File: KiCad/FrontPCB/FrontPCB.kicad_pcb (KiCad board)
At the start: 2 copper layers, 38.1 x 38.1 mm, 18 parts, among them U1 ESP32-S3-WROOM-1

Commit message: CHG: changed wiring of front PCB
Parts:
- removed C1, C3, C5, C7: 0.1µF, Capacitor_SMD:C_0805_2012Metric
- moved R1 41.2 mm to (121.9, 54.6), turned to 90 degrees
- moved C8 27.4 mm to (108.0, 58.4), turned to 180 degrees
- moved C2 18.9 mm to (134.6, 55.9), turned to 0 degrees
- moved C6 18.2 mm to (106.7, 83.8), turned to 180 degrees
- moved C4 14.2 mm to (133.3, 81.3), turned to 0 degrees
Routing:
- net +3.3V: track 64.9 -> 109.2 mm
- net GND: track 98.8 -> 125.9 mm
- net unconnected-(R1-Pad1): track 0.00 -> 5.44 mm
- net Net-(D1-DIN): track 0.00 -> 4.10 mm

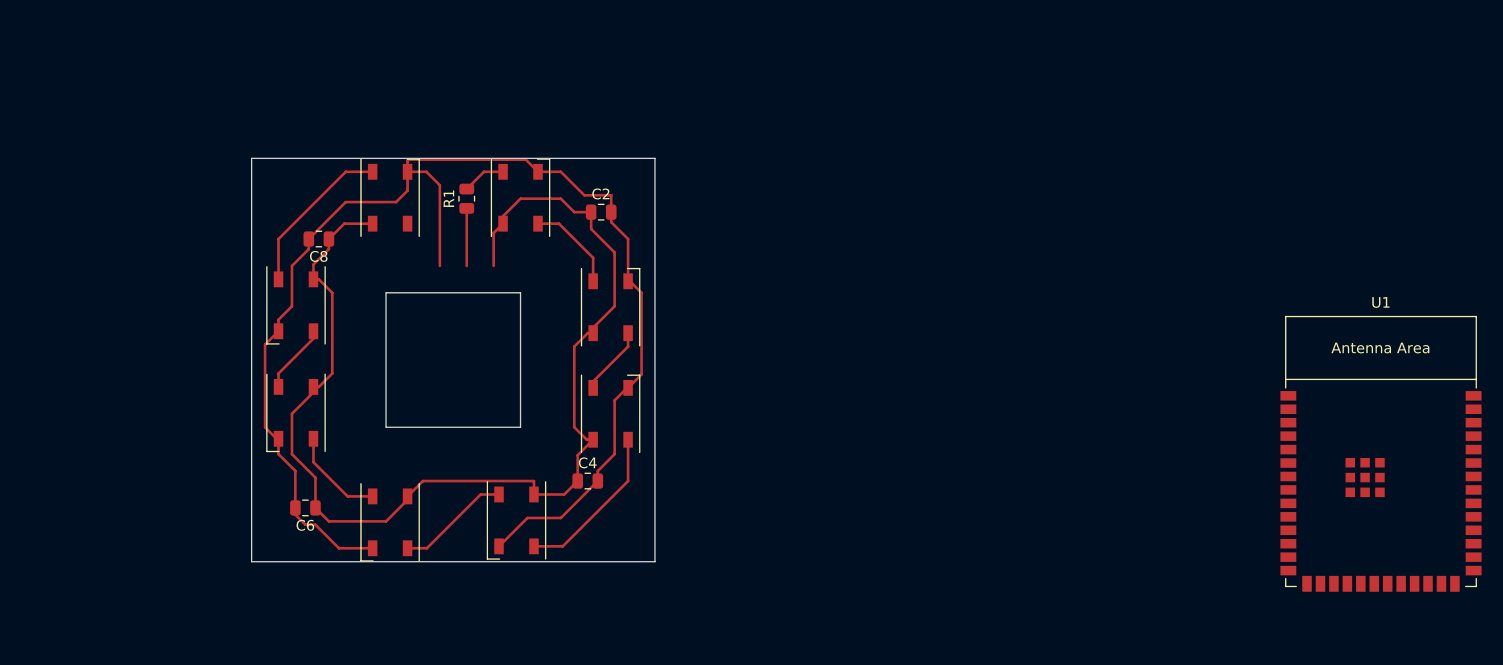
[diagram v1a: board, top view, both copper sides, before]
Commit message: CHG: components of FrontPCB added
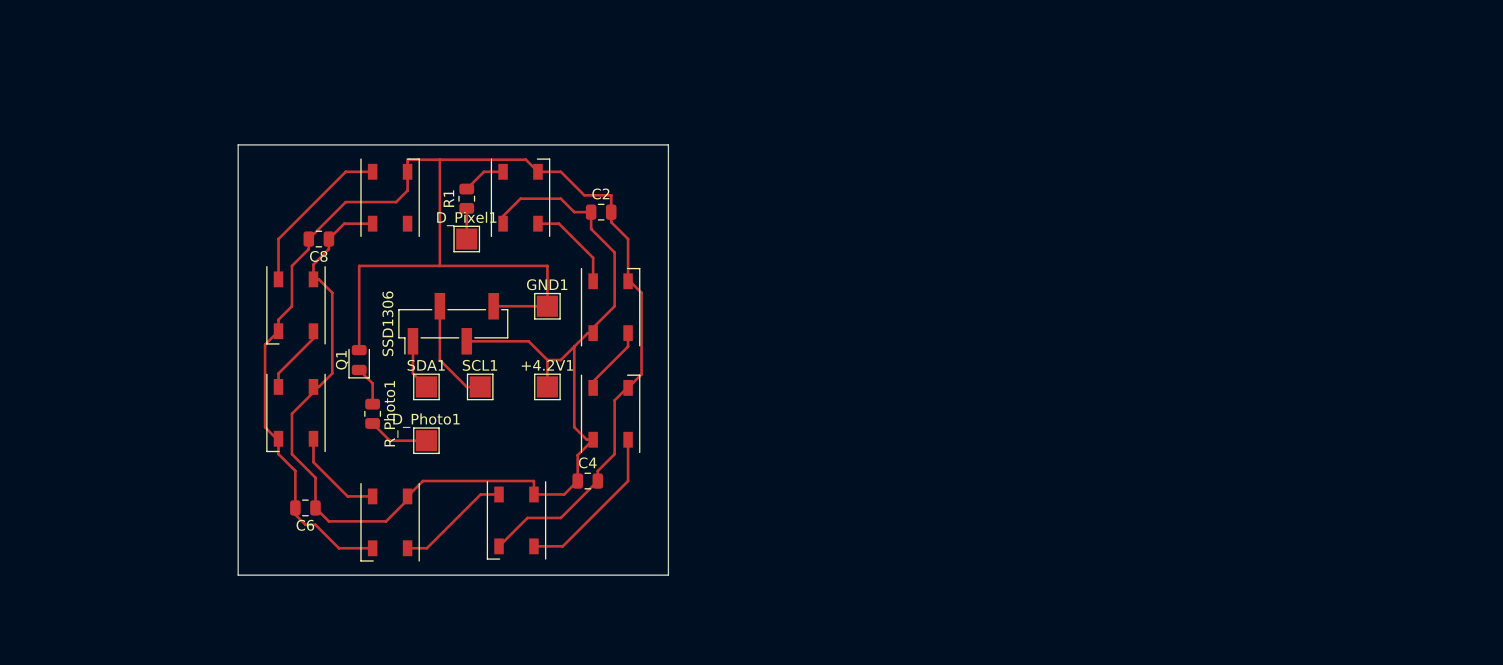
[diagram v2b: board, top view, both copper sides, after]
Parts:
- removed U1: ESP32-S3-WROOM-1, PCM_Espressif:ESP32-S3-WROOM-1
- added +4.2V1: TestPoint, TestPoint:TestPoint_Pad_2.0x2.0mm, F.Cu at (129.5, 72.4)
- added D_Photo1: TestPoint, TestPoint:TestPoint_Pad_2.0x2.0mm, F.Cu at (118.1, 77.5)
- added D_Pixel1: TestPoint, TestPoint:TestPoint_Pad_2.0x2.0mm, F.Cu at (121.9, 58.4)
- added GND1: TestPoint, TestPoint:TestPoint_Pad_2.0x2.0mm, F.Cu at (129.5, 64.8)
- added Q1: Q_Photo_NPN, LED_SMD:LED_0805_2012Metric, F.Cu at (111.8, 69.8)
- added R_Photo1: ?, Resistor_SMD:R_0805_2012Metric, F.Cu at (113.0, 74.9)
- added SCL1: TestPoint, TestPoint:TestPoint_Pad_2.0x2.0mm, F.Cu at (123.2, 72.4)
- added SDA1: TestPoint, TestPoint:TestPoint_Pad_2.0x2.0mm, F.Cu at (118.1, 72.4)
- added SSD1306: Conn_01x04_Pin, Connector_PinHeader_2.54mm:PinHeader_1x04_P2.54mm_Vertical_SMD_Pin1Left, F.Cu at (120.7, 66.4)
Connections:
- net +3.3V renamed Net-(D1-VDD)
- net GND renamed Net-(D1-VSS)
- R1 pad 1: unconnected-(R1-Pad1) -> Net-(D_Pixel1-Pad1)
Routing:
- net Net-(D1-VSS): track 125.9 -> 159.3 mm
- net Net-(SSD1306-Pin_2): track 0.00 -> 9.94 mm
- net Net-(D1-VDD): track 109.2 -> 118.8 mm
- net Net-(D_Photo1-Pad1): track 0.00 -> 5.75 mm
- net unconnected-(R1-Pad1): track 5.44 -> 0.00 mm
- net Net-(SSD1306-Pin_1): track 0.00 -> 4.84 mm
- net Net-(Q1-C): track 0.00 -> 3.76 mm
- net Net-(D_Pixel1-Pad1): track 0.00 -> 2.90 mm
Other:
- board size 38.1 x 38.1 mm -> 40.6 x 40.6 mm
